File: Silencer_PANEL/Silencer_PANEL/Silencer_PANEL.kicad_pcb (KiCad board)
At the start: 2 copper layers, 50 x 200 mm, 20 parts

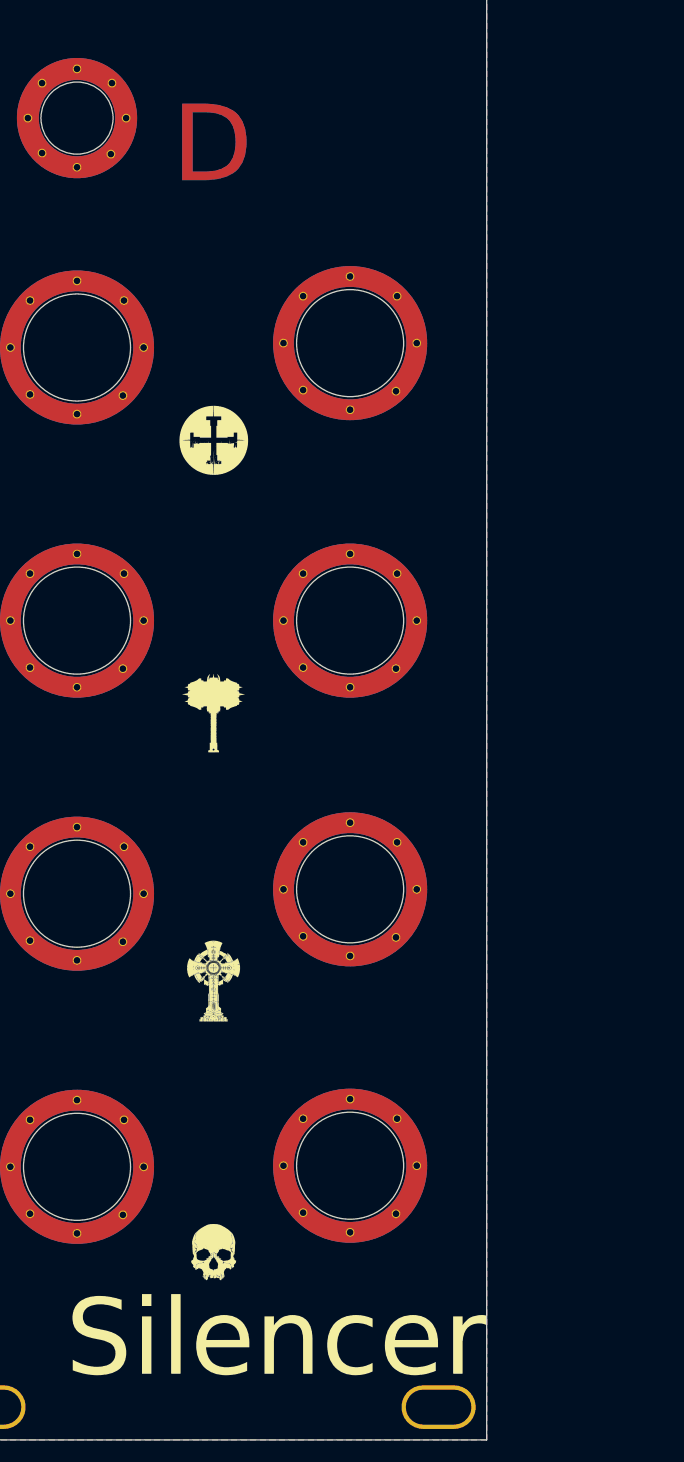
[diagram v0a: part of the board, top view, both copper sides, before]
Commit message: Moved "silencer" text to copper layer
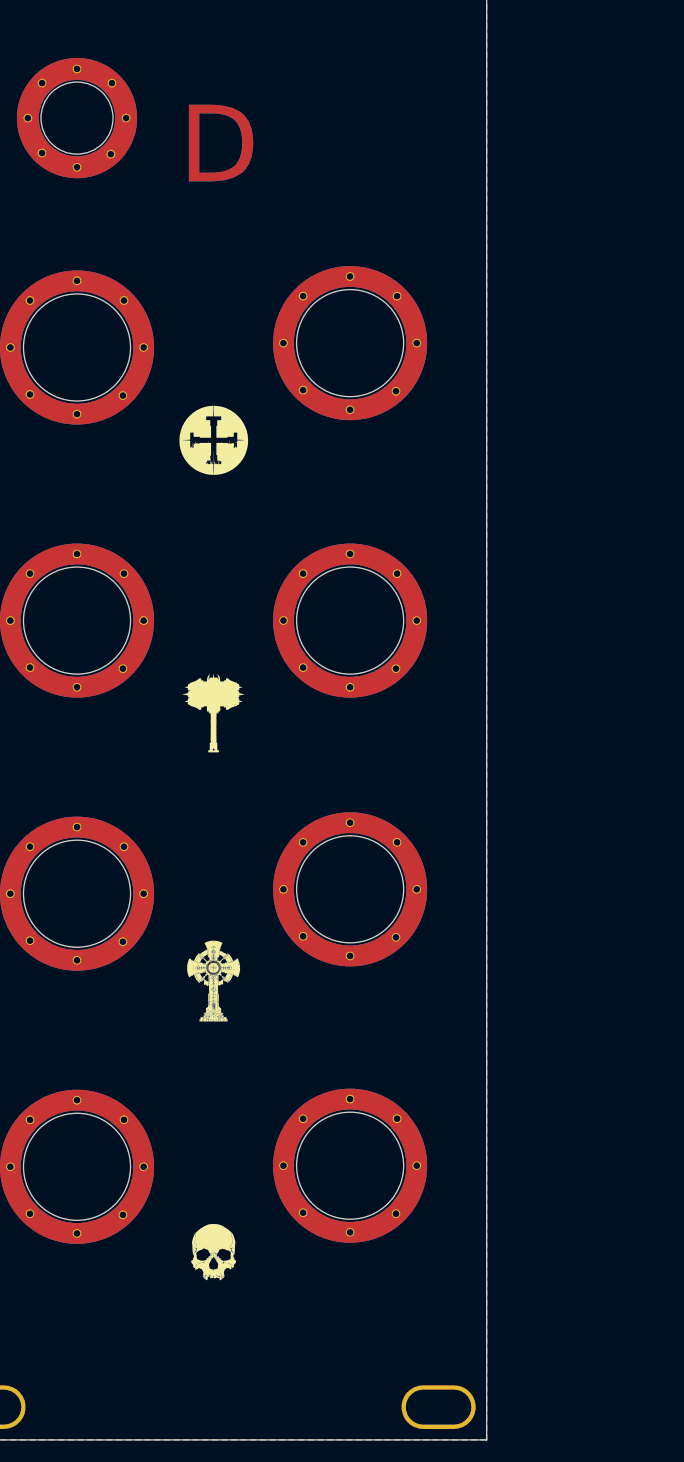
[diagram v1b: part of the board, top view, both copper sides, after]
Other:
- board text added: "Panel design by Christopher Grace Original design by DivKid/Befaco CC0 1.0 ?? 2021 JLCJLCJLCJLC"
- board text removed: "Panel design by Christopher Grace CC0 1.0 ?? 2021 JLCJLCJLCJLC"

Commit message: Refactor Top and Bottom Schematics.
Had to move input/output jacks to bottom board.  This required a full refactoring of both and will mean re-doing the pcb layout of the top board.
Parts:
- moved G*** 87.7 mm to (24.5, 86.5)
- moved G*** 87.7 mm to (25.0, 108.5)
- moved G*** 87.7 mm to (25.0, 183.0)
- moved G*** 87.7 mm to (25.0, 133.5)
- moved G*** 87.7 mm to (25.0, 158.0)
- moved GRAF3 87.7 mm to (10.0, 190.0)
- moved H1 87.7 mm to (12.5, 150.0)
- moved H1 87.7 mm to (12.5, 100.0)
- moved H10 87.7 mm to (47.0, 3.00)
- moved H2 87.7 mm to (12.5, 175.0)
- moved H2 87.7 mm to (12.5, 125.0)
- moved H3 87.7 mm to (37.5, 149.6)
- moved H3 87.7 mm to (37.5, 99.6)
- moved H4 87.7 mm to (37.5, 174.9)
- moved H4 87.7 mm to (37.5, 125.0)
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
